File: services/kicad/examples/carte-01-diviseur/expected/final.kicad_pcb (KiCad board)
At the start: 2 copper layers, 25 x 20 mm, 5 parts, among them J1 IN

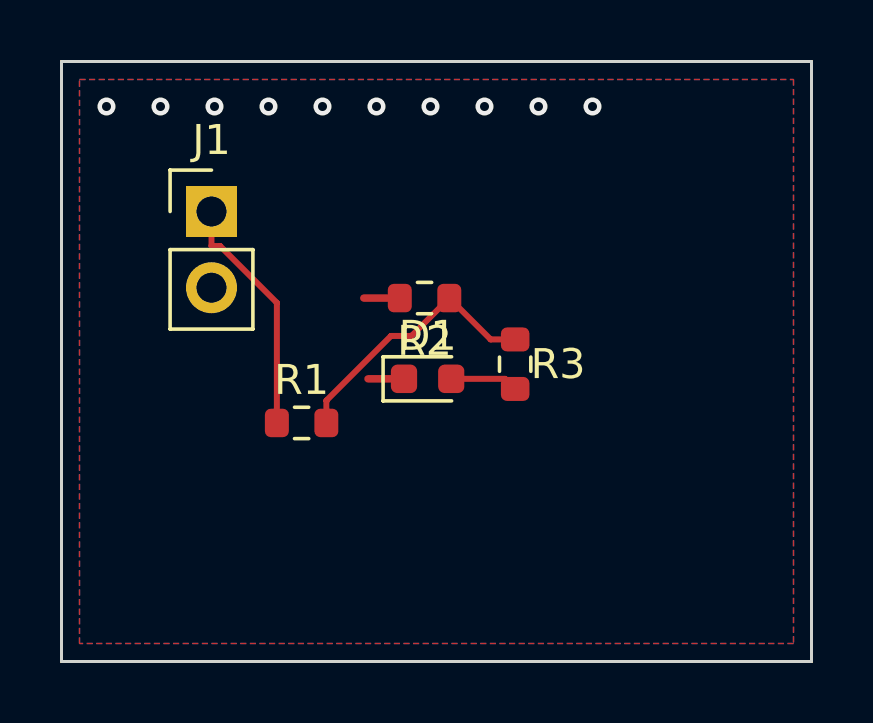
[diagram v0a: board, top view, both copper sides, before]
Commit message: fix(routing): GND route par defaut, plan sur reglage -- sites et tests alignes
Quatre sites de routing.py lisaient encore `_nets_confies_au_plan()` au
lieu de la constante `_NETS_CONFIES_AU_PLAN` que le module reaffecte et que
les tests remplacent : le reglage n atteignait pas ces sites. L escalade
n avait plus de repli vers `_NETS_DE_PLAN_CONNUS` (une connexion GND
manquante doit pouvoir escalader quand GND est route).

Tests encodant l ancienne strategie (GND confie au plan) recrits : les deux
cas sont couverts, GND route par defaut (decision utilisateur du 2026-09-10,
reference STM32 Astra + docs/methodologie-routage.md) et GND confie au plan
sur le reglage `gnd_confie_au_plan`.

`_reattribuer_les_decouplages` rend intact ce qui n est pas une liste.
Deux tests de journal Freerouting comparaient un chemin Windows a un
entrypoint POSIX : `as_posix()`.

Cartes 01, 02, 03, 04, 06 regenerees avec GND route : 100 % routees,
0 erreur DRC, fabricables ; placement.kicad_pcb livre pour chacune.

1630 passed, 2 skipped.

Co-Authored-By: Claude Fable 5.1 <noreply@anthropic.com>
Claude-Session: https://claude.ai/code/session_01TnMqm4La2CxQHHB5K8aSSV
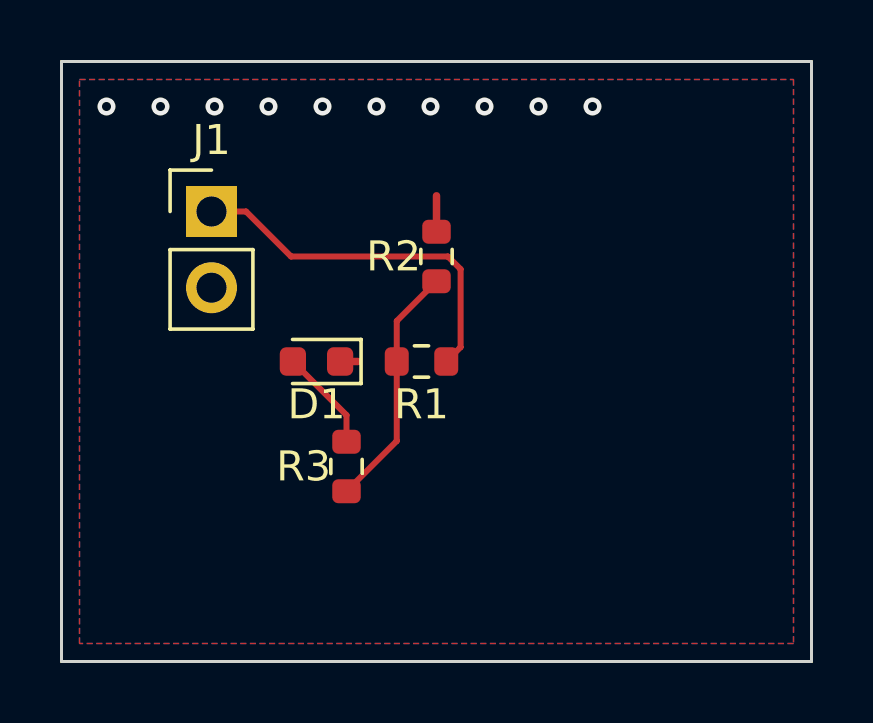
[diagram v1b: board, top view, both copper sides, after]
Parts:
- moved R3 6.58 mm to (145.5, 108.5), turned to 90 degrees
- moved R1 4.49 mm to (148.0, 105.0), turned to 180 degrees
- moved D1 3.75 mm to (144.5, 105.0), turned to 180 degrees
- moved R2 1.44 mm to (148.5, 101.5), turned to 90 degrees
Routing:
- net VIN: track 8.12 -> 12.4 mm
- net LED_A: track 2.27 -> 3.42 mm
- net MID: track 9.02 -> 8.24 mm
- net GND: track 2.40 -> 1.80 mm
